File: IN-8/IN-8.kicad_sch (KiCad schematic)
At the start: 63 parts, among them J1 USB_C_Receptacle_USB2.0, Q1 MMBTA92, Q10 MMBTA42, Q11 MMBTA42, Q12 MMBTA42, Q13 MMBTA42, Q14 MMBTA92, Q15 10N20L, Q2 MMBTA42, Q3 MMBTA42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

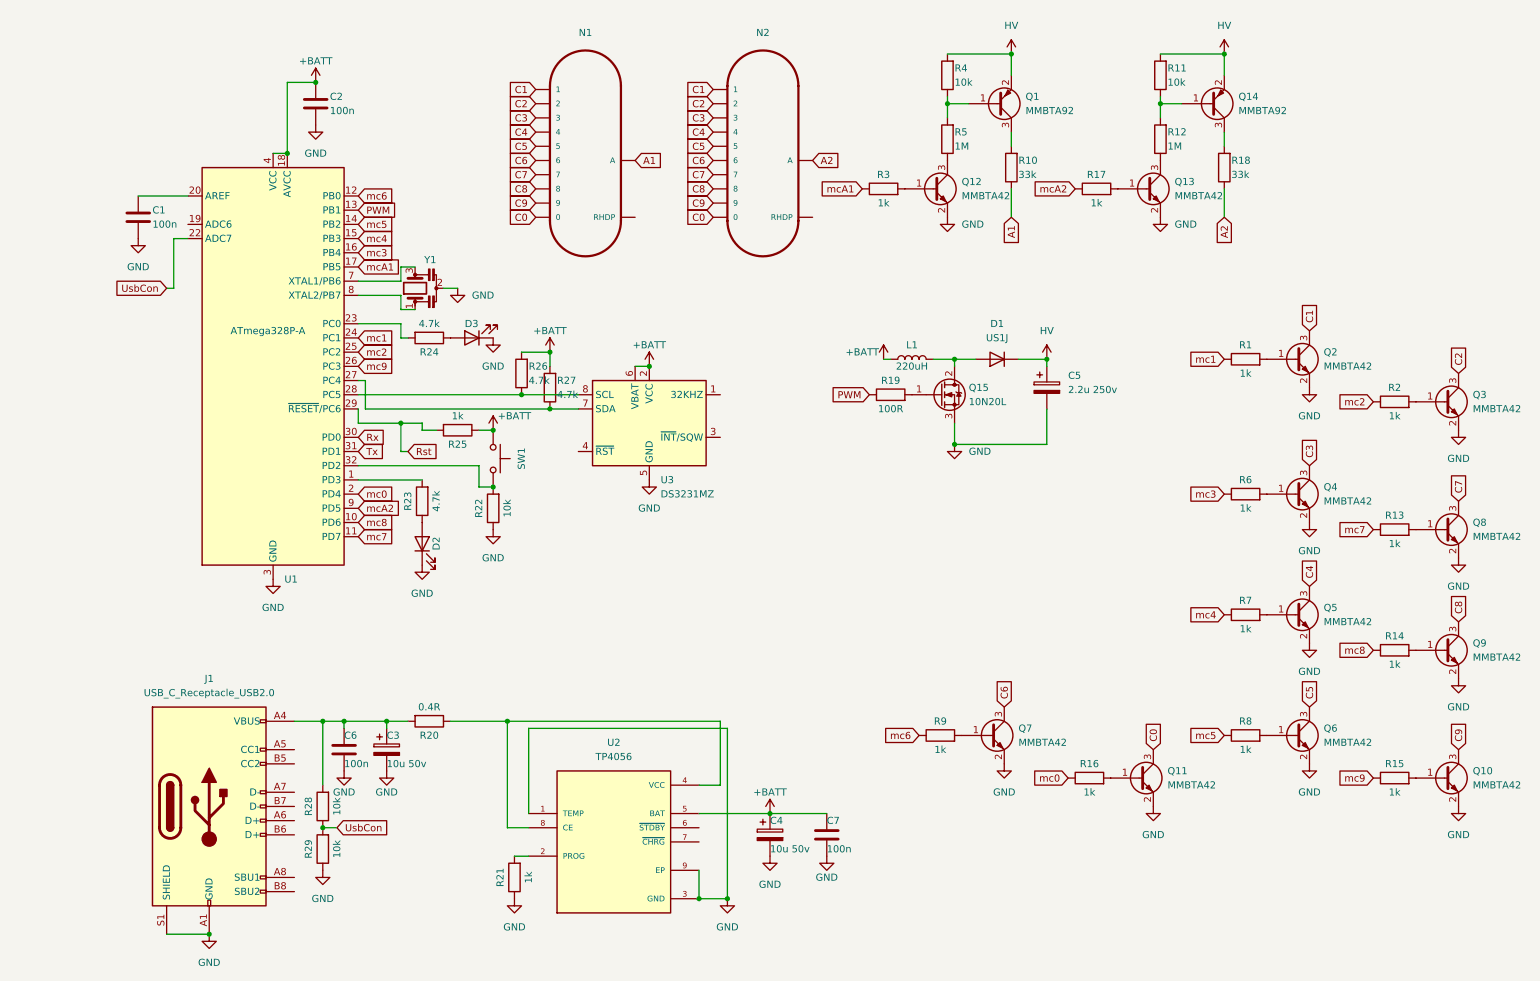
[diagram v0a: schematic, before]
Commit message: KiCad project updaated, gitignore added
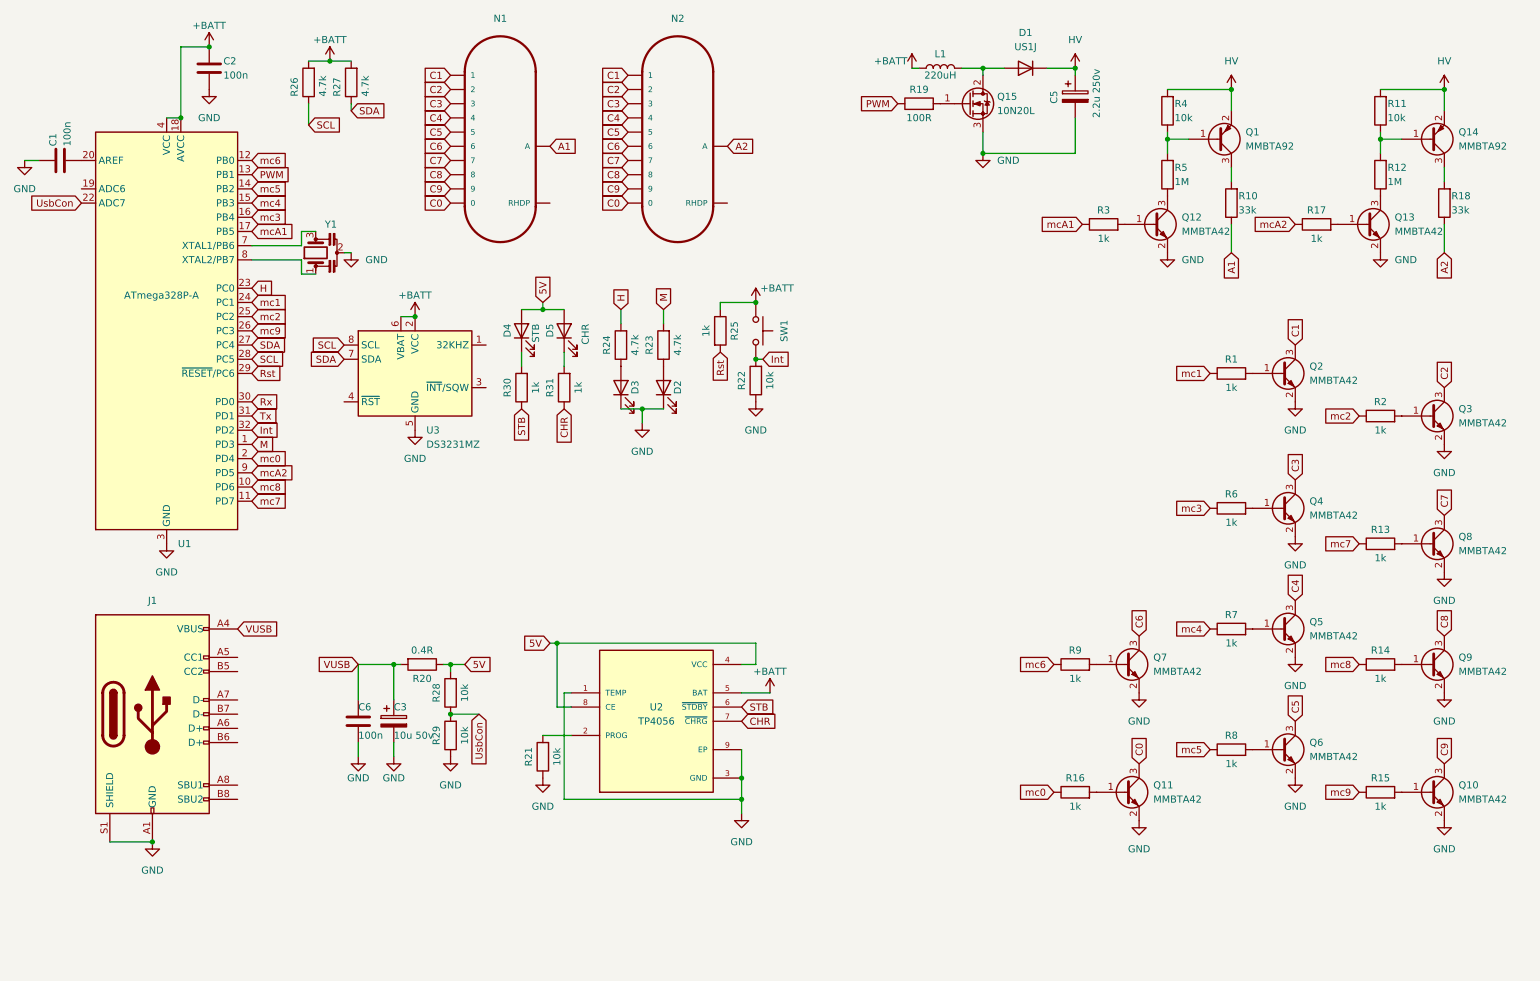
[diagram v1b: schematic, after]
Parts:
- removed C4: 10u 50v, Capacitor_THT:CP_Radial_D5.0mm_P2.00mm, symbol Device:C_Polarized
- removed C7: 100n, Capacitor_SMD:C_0805_2012Metric, symbol Device:C
- added D4: STB, LED_SMD:LED_0805_2012Metric, symbol Device:LED
- added D5: CHR, LED_SMD:LED_0805_2012Metric, symbol Device:LED
- added R30, R31: 1k, Resistor_SMD:R_0805_2012Metric, symbol Device:R
- R21: value 1k -> 10k
- U2: footprint TP4056:SOP127P600X175-9N -> SOP127P600X175-9N
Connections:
- net GND: now also C1.1; no longer C1.2
- net Int: now reaches R22.2, SW1.2, U1.32 (PD2)
- net VUSB: now reaches C3.1, C6.1, J1.A4 (VBUS), J1.A9 (VBUS), J1.B4 (VBUS), J1.B9 (VBUS), R20.2
- net VUSB: no longer R28.2
- net at U1.20 (AREF): now also C1.2; no longer C1.1
- net M: now reaches R23.2, U1.1 (PD3)
- net SDA: now reaches R27.1, U1.27 (PC4), U3.7 (SDA)
- net SCL: now reaches R26.1, U1.28 (PC5), U3.8 (SCL)
- net H: now reaches R24.2, U1.23 (PC0)
- net 5V: now reaches R20.1, U2.4 (VCC), U2.8 (CE)
- net 5V: now also R28.2, D4.2 (A), D5.2 (A)
- net STB: now reaches U2.6 (~{STDBY})
- net STB: now also R30.1
- net CHR: now reaches U2.7 (~{CHRG})
- net CHR: now also R31.1
- new net: D5.1 (K), R31.2
- new net: D4.1 (K), R30.2
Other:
- moved on the sheet: C1, C2, C3, C5, C6, D1, D2, D3, J1, L1, N1, N2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
